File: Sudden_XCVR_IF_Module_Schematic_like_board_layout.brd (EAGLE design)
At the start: 160 x 100 mm, 25 parts

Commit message: Lots of changes.
Recreated the IF Schema and a new board to look like the photo

On branch master
Changes to be committed:
       modified:   Receiver RF Amplifier Stage.b#1
       modified:   Receiver RF Amplifier Stage.b#2
       modified:   Receiver RF Amplifier Stage.b#3
       modified:   Receiver RF Amplifier Stage.b#4
       modified:   Receiver RF Amplifier Stage.b#5
       modified:   Receiver RF Amplifier Stage.b#6
       modified:   Receiver RF Amplifier Stage.b#7
       modified:   Receiver RF Amplifier Stage.b#8
       modified:   Receiver RF Amplifier Stage.b#9
       modified:   Receiver RF Amplifier Stage.brd
       modified:   Receiver RF Amplifier Stage.s#1
       modified:   Receiver RF Amplifier Stage.s#2
       modified:   Receiver RF Amplifier Stage.s#3
       modified:   Receiver RF Amplifier Stage.s#4
       modified:   Receiver RF Amplifier Stage.s#5
       modified:   Receiver RF Amplifier Stage.s#6
       modified:   Receiver RF Amplifier Stage.s#7
       modified:   Receiver RF Amplifier Stage.s#8
       modified:   Receiver RF Amplifier Stage.s#9
       modified:   Receiver RF Amplifier Stage.sch
       modified:   Sudden_XCVR_IF_Module.b#1
       modified:   Sudden_XCVR_IF_Module.b#2
       modified:   Sudden_XCVR_IF_Module.b#3
       modified:   Sudden_XCVR_IF_Module.b#4
       modified:   Sudden_XCVR_IF_Module.b#5
       modified:   Sudden_XCVR_IF_Module.b#6
       modified:   Sudden_XCVR_IF_Module.b#7
       modified:   Sudden_XCVR_IF_Module.brd
       new file:   Sudden_XCVR_IF_Module_Schematic_like_board_layout.b#1
       new file:   Sudden_XCVR_IF_Module_Schematic_like_board_layout.b#2
       new file:   Sudden_XCVR_IF_Module_Schematic_like_board_layout.b#3
       new file:   Sudden_XCVR_IF_Module_Schematic_like_board_layout.brd
       new file:   Sudden_XCVR_IF_Module_Schematic_like_board_layout.s#1
       new file:   Sudden_XCVR_IF_Module_Schematic_like_board_layout.s#2
       new file:   Sudden_XCVR_IF_Module_Schematic_like_boa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
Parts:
- removed H1, H4: MOUNT-PAD-SQUARE4.5, jim_muppet_parts:PAD-SQUARE
- removed H2, H3: (no value), jim_muppet_parts:PAD-SQUARE
- removed P+2: +6V, jim_muppet_parts:POWER-IN-PAD
- added 78L05, LM7806: (no value), jim_muppet_parts:78XXL
- added A, CLK1: A, jim_muppet_parts:POWER-IN-PAD
- added B, SUPPLY1: B, jim_muppet_parts:POWER-IN-PAD
- added CLK0: LO, jim_muppet_parts:POWER-IN-PAD
- added CLK2: CLK2, jim_muppet_parts:POWER-IN-PAD
- added K1, K2: REL-G5V1, jim_muppet_parts:G5V1
- added K3: RELAY-DPDT, jim_muppet_parts:G5V-2
- L1, L2: value 1000uH/1mH molded choke -> 1000uH/1mH choke
- P+1: value +6V -> +12V
- moved P+1 223.5 mm to (-29.2, -44.5)
- moved C12 136.9 mm to (15.2, 92.7), turned to 0 degrees
- moved Q1 126.8 mm to (54.6, 139.7), turned to 0 degrees
- moved L5 109.6 mm to (36.8, 124.5), turned to 90 degrees
- moved C2 109.2 mm to (22.9, 139.7), turned to 270 degrees
- moved C7 106.6 mm to (83.8, 130.8)
- moved C9 100.8 mm to (77.5, 99.1)
- moved L3 93.7 mm to (71.1, 124.5), turned to 90 degrees
- moved C3 89.2 mm to (71.1, 111.8), turned to 270 degrees
- moved C8 88.7 mm to (83.8, 99.1), turned to 90 degrees
- moved IC2 88.1 mm to (82.5, 115.6), turned to 180 degrees
- moved C6 86.4 mm to (88.9, 130.8), turned to 270 degrees
- moved C1 80.4 mm to (29.2, 139.7), turned to 90 degrees
- moved IC1 73.1 mm to (26.7, 118.1), turned to 180 degrees
- moved L2 69.9 mm to (66.0, 90.2), turned to 270 degrees
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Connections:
- removed net +5V: C11.1, C12.1, L1.2, L2.2, P+1.VCC, P+2.VCC
- removed net N$22: C1.1, H1.PAD
- new net +12V: 78L05.IN, LM7806.IN, P+1.VCC
- new net +6VDC: C11.1, C12.1, L1.2, L2.2, LM7806.OUT
- new net 3.3V: B.VCC, C8.1, K3.8, SUPPLY1.VCC
- new net A: A.VCC, C4.1, CLK0.VCC, CLK1.VCC, K3.6, K3.9
- new net BFO: CLK2.VCC, K3.11
- net GND: now also 78L05.GND, K3.16, L5.P$1, LM7806.GND; no longer L5.P$2
- net N$14: now also L5.P$2; no longer L5.P$1
- net N$19: now also C1.1, K2.5; no longer C4.1, H2.PAD
- net N$20: now also K1.6; no longer H4.PAD
- net N$6: now also 78L05.OUT, K3.1; no longer C8.1, H3.PAD
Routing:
- net N$1: track 70.7 -> 0.00 mm
- net N$4: track 34.4 -> 0.00 mm, vias 1 -> 0
- net N$16: track 32.2 -> 0.00 mm
- net +5V: track 25.4 -> 0.00 mm
- net N$14: track 22.4 -> 0.00 mm
- net N$17: track 17.8 -> 0.00 mm
- net N$3: track 17.3 -> 0.00 mm
- net N$15: track 17.3 -> 0.00 mm
- net N$7: track 17.1 -> 0.00 mm
- net N$2: track 16.5 -> 0.00 mm
- net N$19: track 14.8 -> 0.00 mm
- net N$5: track 13.5 -> 0.00 mm
- net N$13: track 12.2 -> 0.00 mm
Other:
- board size 160 x 100 mm -> 109.2 x 150.8 mm

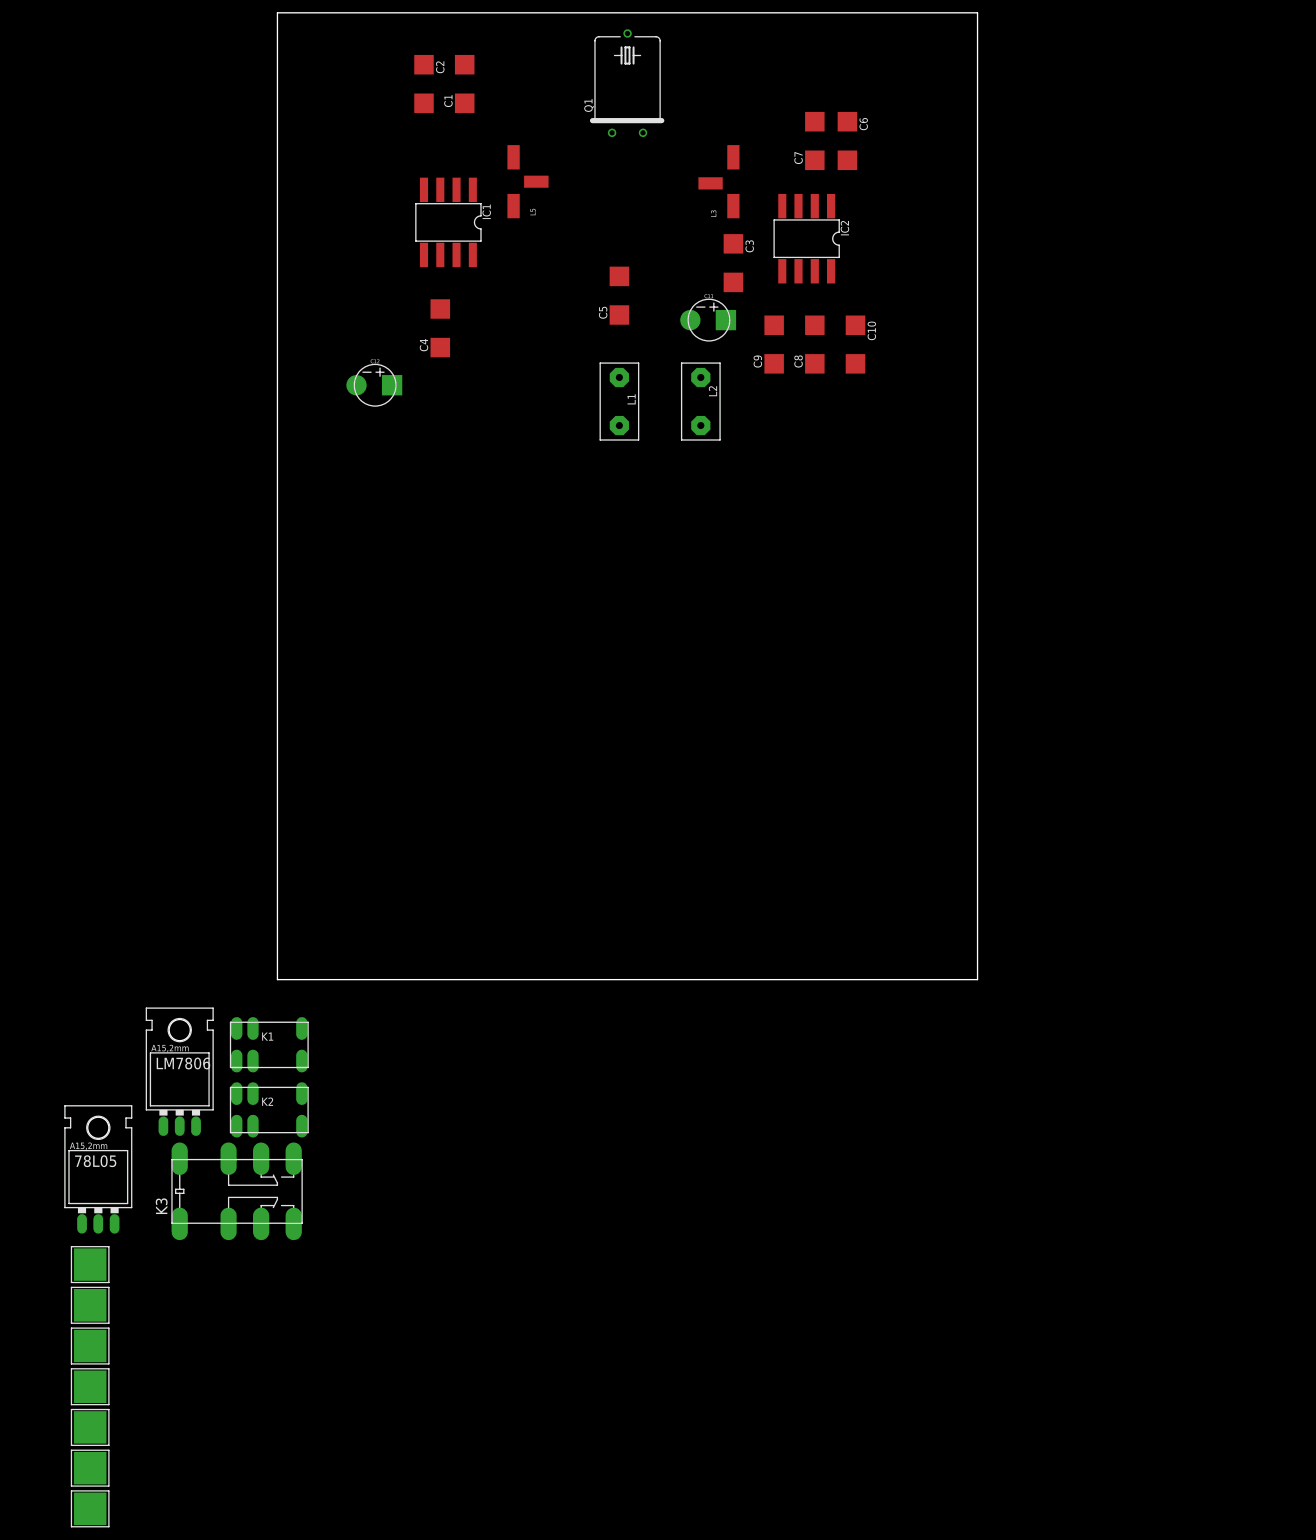
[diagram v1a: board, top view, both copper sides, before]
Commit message: Added additional schematics and board layout
Added additional schmentics and board layout for Driver stage and a new IF schematic and board
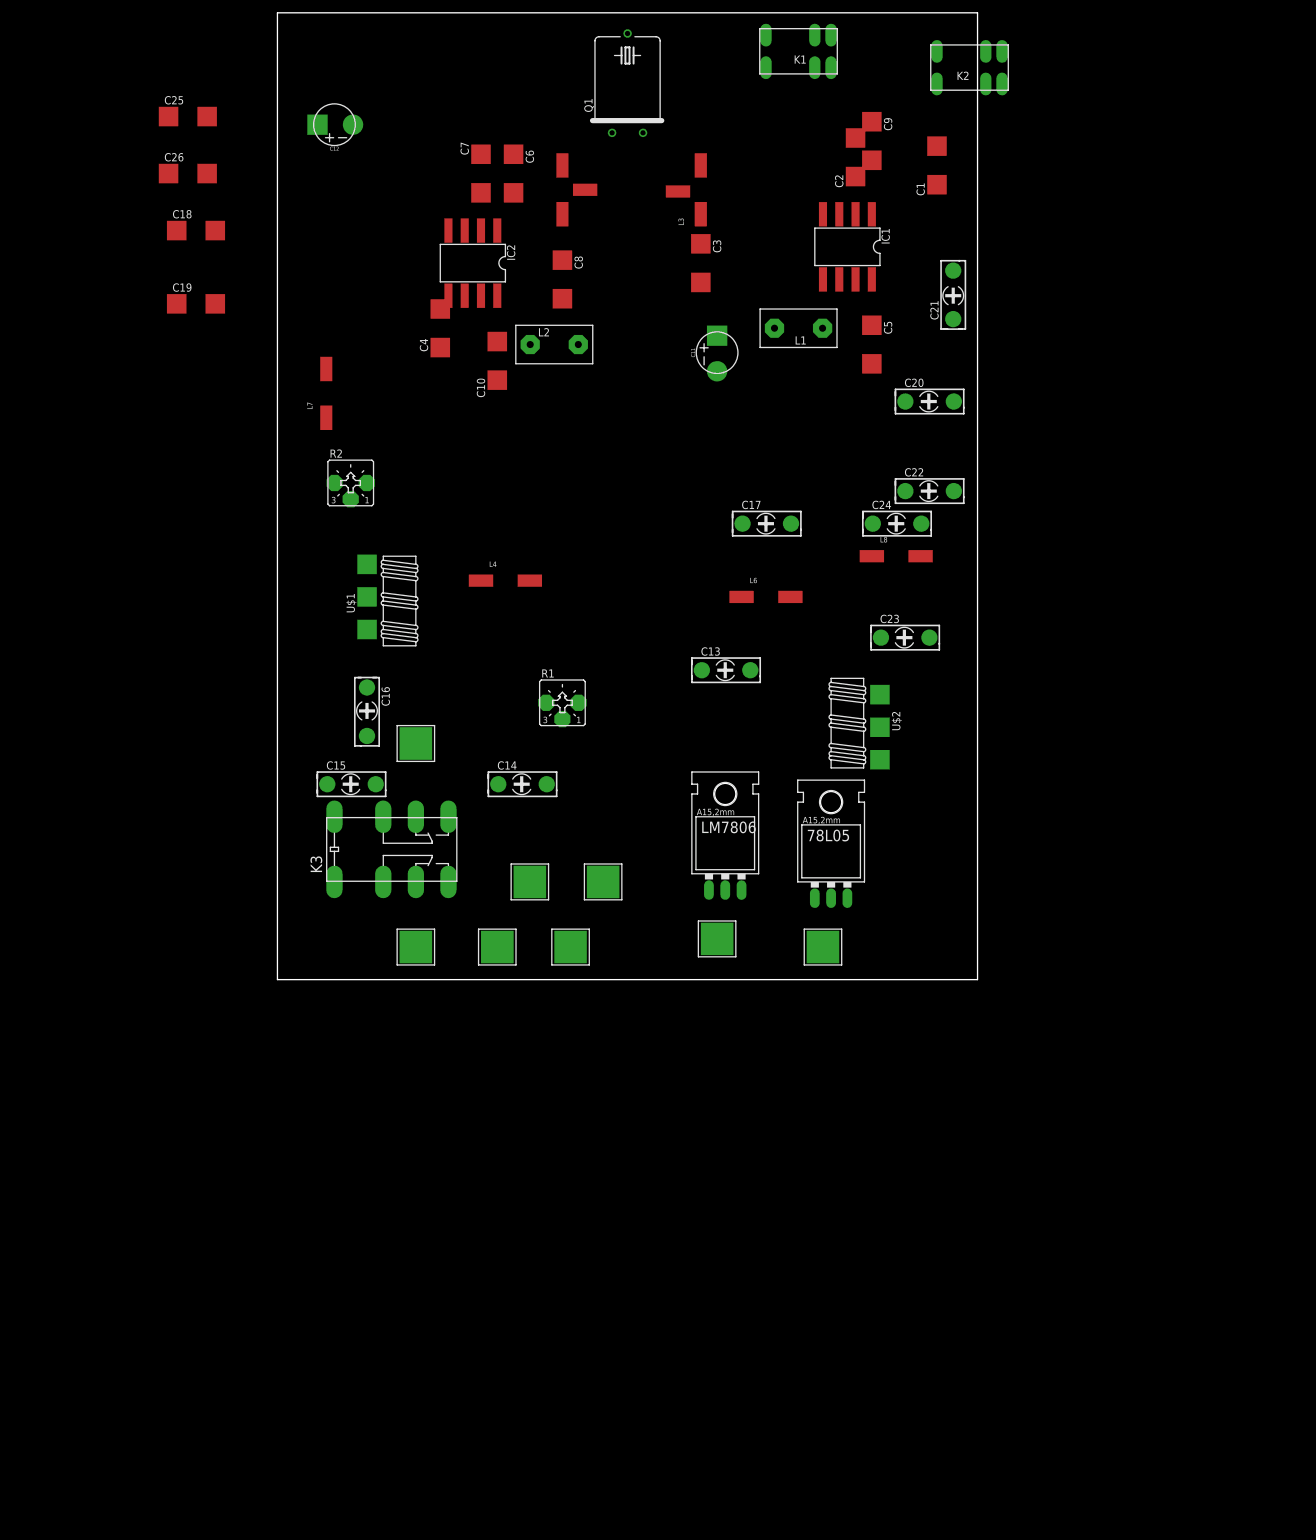
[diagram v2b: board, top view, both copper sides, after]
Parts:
- added C13, C14, C15, C17, C20, C21, C22, C24: (no value), jim_muppet_parts:CAP-TRIMM
- added C16, C23: 47pF, jim_muppet_parts:CAP-TRIMM
- added C18, C19, C25, C26: Set 0.0uF, jim_muppet_parts:CAP-MEDIUM-MUPPET
- added L4, L7: 2.2uH, jim_muppet_parts:INDUCTOR_2.2UH
- added L6, L8: 2.28uH, jim_muppet_parts:INDUCTOR_2.2UH
- added P+2: +12V, jim_muppet_parts:POWER-IN-PAD
- added R1, R2: (no value), jim_muppet_parts:POT-TRIMM-4
- added U$1: T37-43_BIFILAR_TORIODBIFILAR-COIL/TRANSFORMER, jim_muppet_parts:T37-43_BIFILAR_TOROID
- added U$2: BIFILAR_TORIOD, jim_muppet_parts:T37-43_BIFILAR_TOROID
- L5: value INDUCTOR-TAPPED-MIRROREDINDUCTOR_TAPPED_MIRRORED -> INDUCTOR-TAPPED
- moved K2 195.8 mm to (108.0, 142.2), turned to 180 degrees
- moved K1 175.6 mm to (81.3, 144.8), turned to 180 degrees
- moved SUPPLY1 126.4 mm to (50.8, 15.2)
- moved 78L05 125.1 mm to (86.4, 16.5)
- moved P+1 124.6 mm to (85.1, 5.08)
- moved B 114.3 mm to (39.4, 15.2), turned to 180 degrees
- moved CLK1 106.0 mm to (45.7, 5.08)
- moved CLK2 101.3 mm to (21.6, 36.8)
- moved A 93.5 mm to (34.3, 5.08)
- moved LM7806 92.7 mm to (69.8, 17.8)
- moved CLK0 80.3 mm to (21.6, 5.08)
- moved C1 74.7 mm to (102.9, 127.0), turned to 270 degrees
- moved C2 68.3 mm to (90.2, 128.3)
- moved IC1 62.3 mm to (88.9, 114.3)
- moved K3 58.5 mm to (17.8, 20.3)
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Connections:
- new net N$21: C15.+, C16.-, C17.-, L6.P$2
- new net N$22: C14.-, R1.E
- new net N$23: C13.-, C14.+, C15.-, L4.P$2
- new net N$24: C23.+, U$2.C1A
- new net N$25: C22.+, C23.-, C24.-, L8.P$2
- new net N$26: C20.-, C21.+, C22.-, L7.P$2
- new net N$27: C21.-, R2.E
- new net N$8: C16.+, U$1.C1A
- net +12V: now also K1.2, K2.9, P+2.VCC
- net GND: now also C13.+, C17.+, C20.+, C24.+, L4.P$1, L6.P$1, L7.P$1, L8.P$1, R1.A, R2.A

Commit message: Updated the IF module - mainly board layout
Updated the IF module - mainly board layout
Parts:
- removed U$1: T37-43_BIFILAR_TORIODBIFILAR-COIL/TRANSFORMER, jim_muppet_parts:T37-43_BIFILAR_TOROID
- removed U$2: BIFILAR_TORIOD, jim_muppet_parts:T37-43_BIFILAR_TOROID
- added A1, A2: A, jim_muppet_parts:POWER-IN-PAD
- added TX1, TX2: ? uH, jim_muppet_parts:TRANSFORMER_TWO_WIRE
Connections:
- new net N$28: K1.9, TX1.C2A
- new net N$29: K1.10, TX1.C2B
- new net N$30: K2.2, TX2.C2B
- new net N$31: K2.1, TX2.C2A
- net 3.3V: now also A1.VCC, A2.VCC, K1.1, K2.10
- net GND: now also TX1.C1B, TX2.C1A
- net N$24: now also TX2.C1B; no longer U$2.C1A
- net N$8: now also TX1.C1A; no longer U$1.C1A
